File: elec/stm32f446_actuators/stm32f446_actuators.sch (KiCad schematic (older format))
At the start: 3 parts, among them J1 Conn_01x02

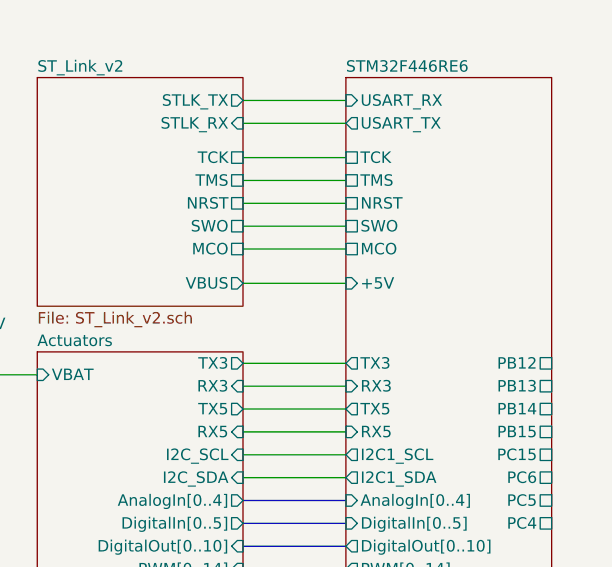
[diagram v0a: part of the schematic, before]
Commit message: GND done, silkscreen done and some minor fixes
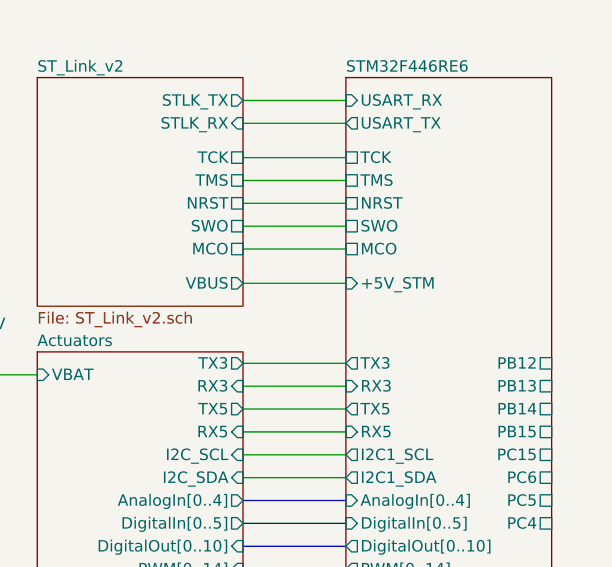
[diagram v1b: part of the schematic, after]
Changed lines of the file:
@@
 F7 "SWO" U L 5300 3700 50
 F8 "MCO" U L 5300 3800 50
-F9 "+5V" I L 5300 3950 50
-F10 "TX3" O L 5300 4300 50
-F11 "RX3" I L 5300 4400 50
-F12 "DigitalIn[0..5]" I L 5300 5000 50
-F13 "RX5" I L 5300 4600 50
-F14 "TX5" O L 5300 4500 50
-F15 "PWM[0..14]" O L 5300 5200 50
-F16 "I2C1_SDA" O L 5300 4800 50
-F17 "I2C1_SCL" O L 5300 4700 50
-F18 "PB12" U R 6200 4300 50
-F19 "PB13" U R 6200 4400 50
-F20 "PB14" U R 6200 4500 50
-F21 "PB15" U R 6200 4600 50
-F22 "PC15" U R 6200 4700 50
-F23 "PC6" U R 6200 4800 50
-F24 "PC5" U R 6200 4900 50
-F25 "PC4" U R 6200 5000 50
-F26 "DigitalOut[0..10]" O L 5300 5100 50
-F27 "AnalogIn[0..4]" I L 5300 4900 50
+F9 "TX3" O L 5300 4300 50
+F10 "RX3" I L 5300 4400 50
+F11 "DigitalIn[0..5]" I L 5300 5000 50
+F12 "RX5" I L 5300 4600 50
+F13 "TX5" O L 5300 4500 50
+F14 "PWM[0..14]" O L 5300 5200 50
+F15 "I2C1_SDA" O L 5300 4800 50
+F16 "I2C1_SCL" O L 5300 4700 50
+F17 "PB12" U R 6200 4300 50
+F18 "PB13" U R 6200 4400 50
+F19 "PB14" U R 6200 4500 50
+F20 "PB15" U R 6200 4600 50
+F21 "PC15" U R 6200 4700 50
+F22 "PC6" U R 6200 4800 50
+F23 "PC5" U R 6200 4900 50
+F24 "PC4" U R 6200 5000 50
+F25 "DigitalOut[0..10]" O L 5300 5100 50
+F26 "AnalogIn[0..4]" I L 5300 4900 50
+F27 "+5V_STM" I L 5300 3950 50
 $EndSheet
 Wire Bus Line
